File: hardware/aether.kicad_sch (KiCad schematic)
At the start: 41 parts, among them Q1 NPN, Q2 CSD17575Q3, Q3 CSD17575Q3, Q4 CSD17575Q3, Q5 CSD17575Q3, U1 USBLC6-2SC6

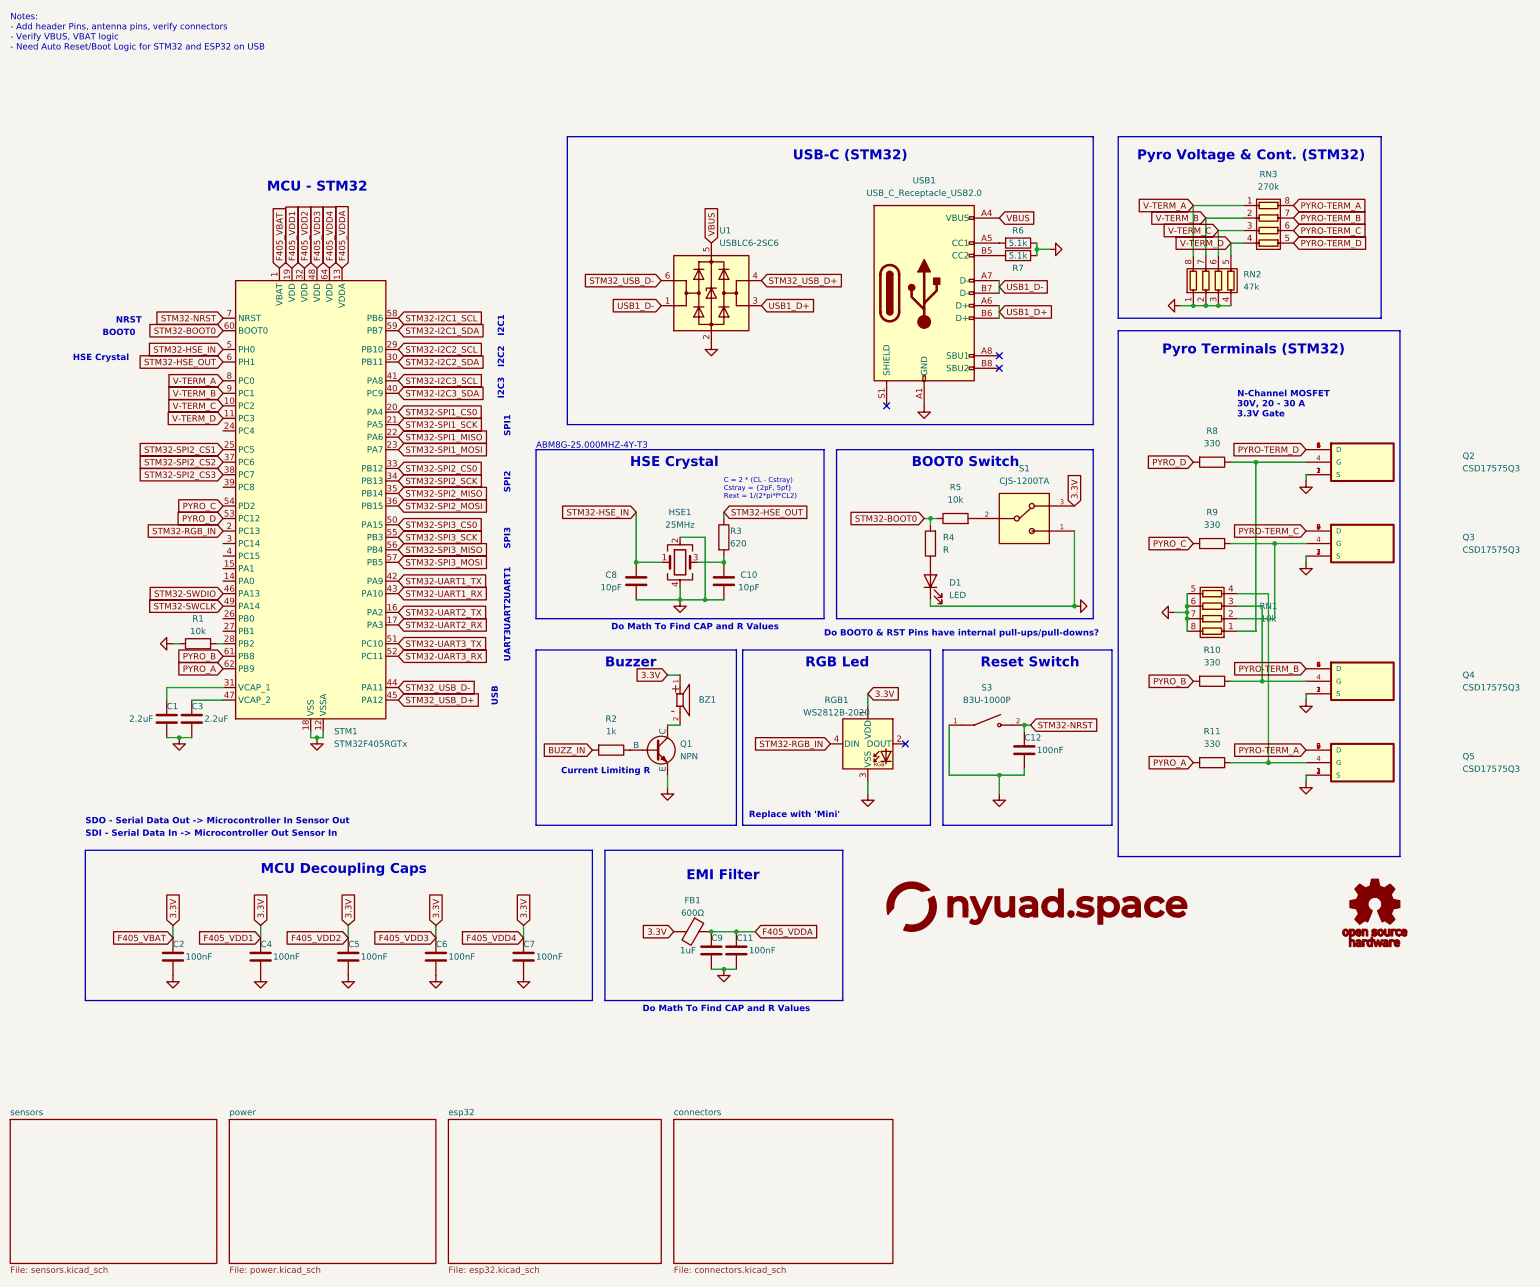
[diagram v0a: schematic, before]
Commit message: added BNO086
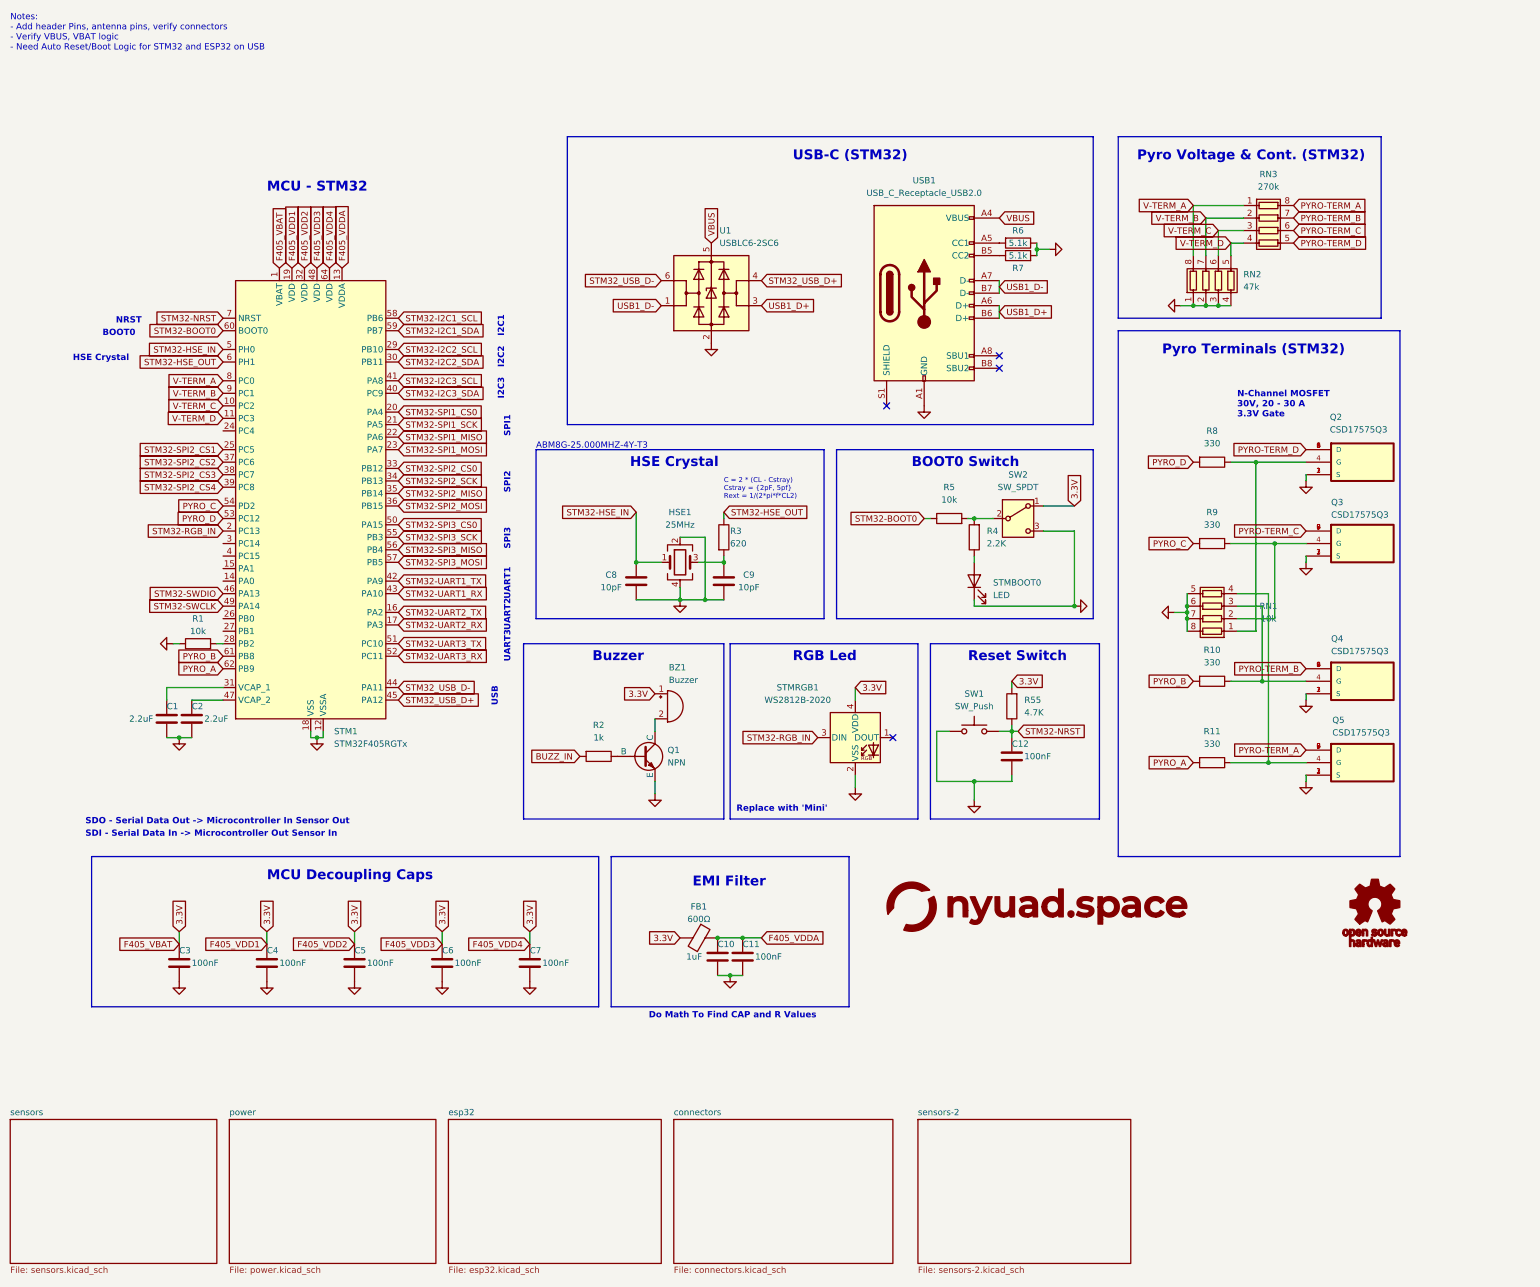
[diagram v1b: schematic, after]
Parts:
- removed BZ1: CSS-0575A-SMT, CSS-0575A-SMT:CUI_CSS-0575A-SMT, symbol CSS-0575A-SMT:CSS-0575A-SMT
- removed RGB1: WS2812B-2020, LED_SMD:LED_WS2812B-2020_PLCC4_2.0x2.0mm, symbol LED:WS2812B
- removed S1: CJS-1200TA, CJS-1200TA:SW_CJS-1200TA, symbol CJS-1200TA:CJS-1200TA
- removed S3: B3U-1000P, B3U-1000P:SW_B3U-1000P, symbol B3U-1000P:B3U-1000P
- added BZ1: Buzzer, symbol Device:Buzzer
- added R55: 4.7K, symbol Device:R
- added STMRGB1: WS2812B-2020, symbol LED:WS2812B-2020
- added SW1: SW_Push, symbol Switch:SW_Push
- added SW2: SW_SPDT, symbol Switch:SW_SPDT
- FB1: footprint Inductor_SMD:L_0402_1005Metric -> (none)
- HSE1: footprint Crystal:Crystal_SMD_Abracon_ABM8G-4Pin_3.2x2.5mm -> (none)
- Q1: footprint Package_TO_SOT_SMD:SOT-23 -> (none)
- Q2, Q3, Q4, Q5: footprint CSD17575Q3:TRANS_CSD17308Q3 -> (none)
- R1, R10, R11, R2, R3, R5, R6, R7, R8, R9: footprint Resistor_SMD:R_0603_1608Metric -> (none)
- R4: value R -> 2.2K; footprint Resistor_SMD:R_0603_1608Metric -> (none)
- RN1: footprint YC164-JR-0710KL:RESCAXE80P320X160X70-8N -> (none)
- RN2: footprint YC164-JR-0747KL:RESCAXE80P320X160X70-8N -> (none)
- RN3: footprint 742C083274JP:RESCAV80P320X160X70-8N -> (none)
- STM1: footprint Package_QFP:LQFP-64_10x10mm_P0.5mm -> (none)
- STMBOOT0: renamed from D1; footprint LED_SMD:LED_0603_1608Metric -> (none)
- U1: footprint Package_TO_SOT_SMD:SOT-23-6 -> (none)
- USB1: footprint Connector_USB:USB_C_Receptacle_GCT_USB4105-xx-A_16P_TopMnt_Horizontal -> (none)
- renumbered C9 to C10, C3 to C2, C2 to C3, C10 to C9
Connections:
- net 3.3V: now also BZ1.1 (+), R55.2, STMRGB1.4 (VDD), SW2.1 (A)
- net GND: now also STMRGB1.2 (VSS), SW1.1, SW2.3 (C)
- net STM32-BOOT0: no longer R4.2
- net STM32-NRST: now also R55.1, SW1.2
- net STM32-RGB_IN: now also STMRGB1.3 (DIN)
- net STM32-SPI2_CS4: now reaches STM1.39 (PC8)
- net at R5.2: now also R4.2, SW2.2 (B)
- net at Q1.1 (C): now also BZ1.2 (-)
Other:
- added sheet sensors-2 (sensors-2.kicad_sch)
- note removed: "Current Limiting R"
- note removed: "Do BOOT0 & RST Pins have internal pull-ups/pull-downs?"
- moved on the sheet: C10, C11, C12, C3, C4, C5, C6, C7, FB1, Q1, R2, R4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

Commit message: rev2 component placement
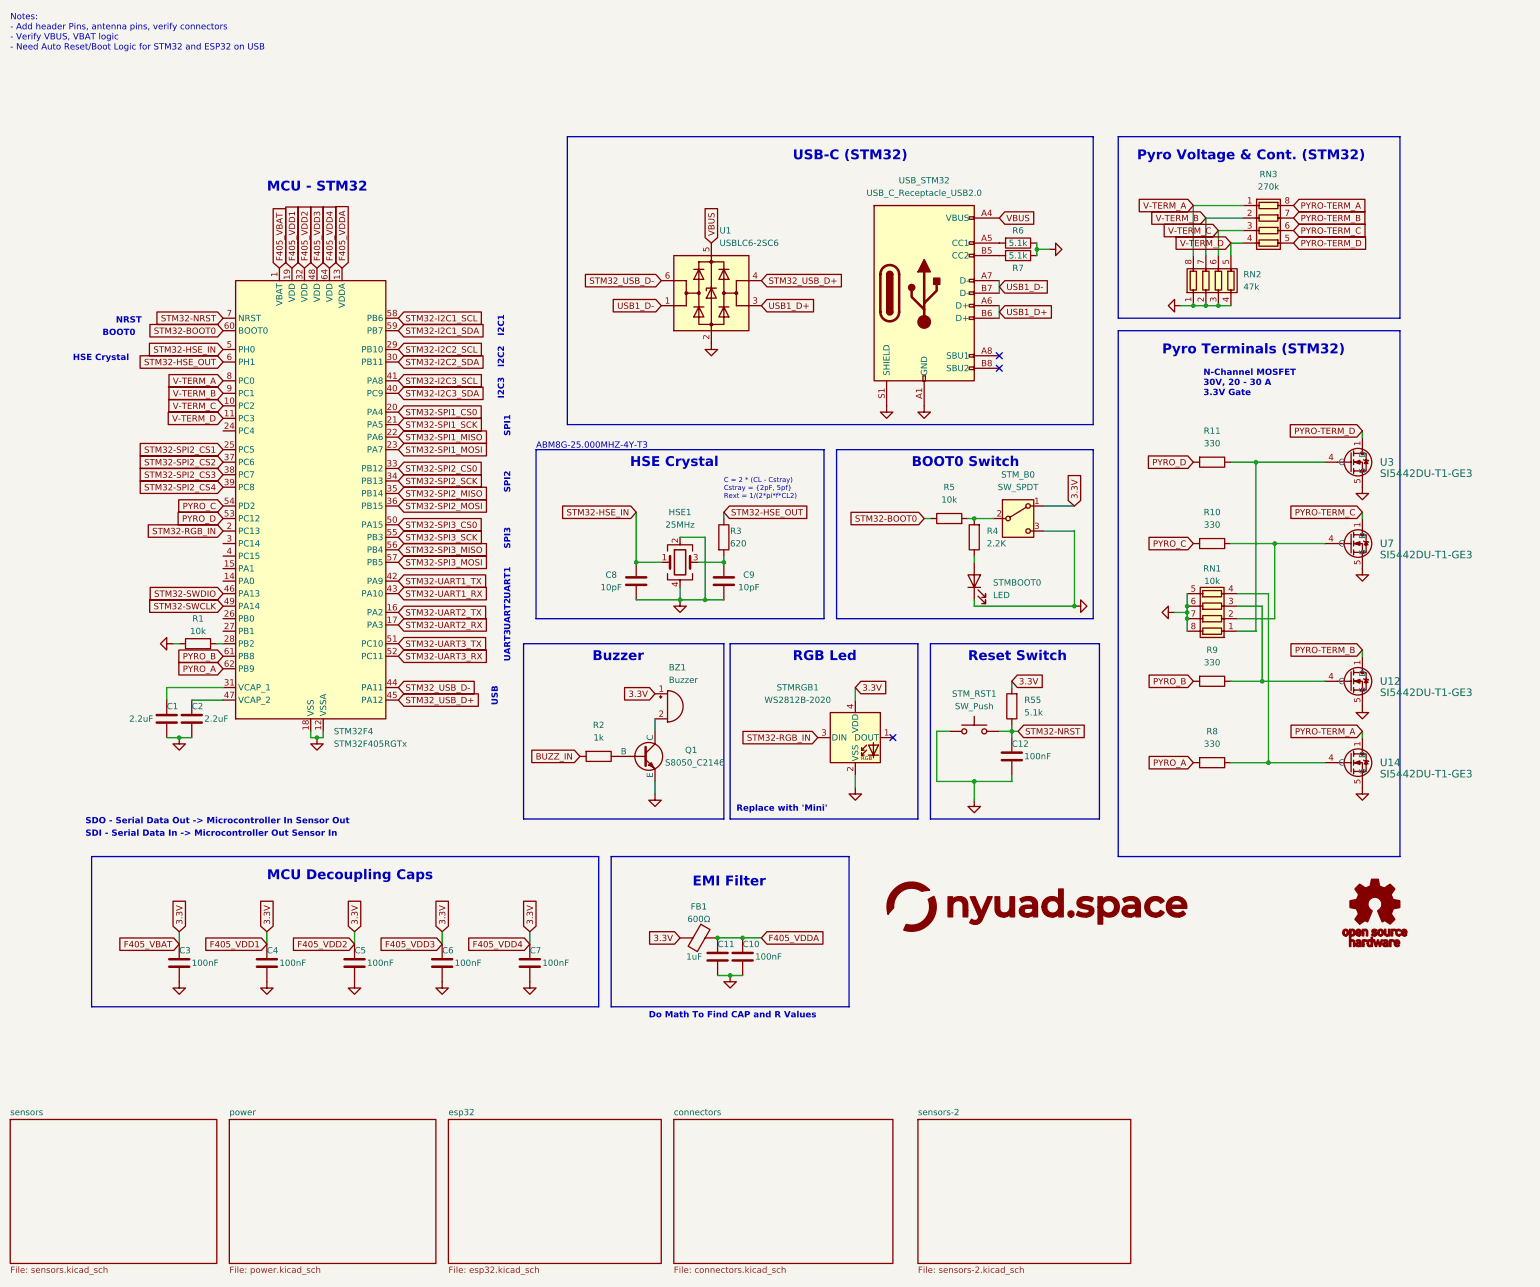
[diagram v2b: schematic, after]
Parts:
- removed Q2, Q3, Q4, Q5: CSD17575Q3, symbol CSD17575Q3:CSD17575Q3
- added U12, U14, U3, U7: SI5442DU-T1-GE3, SI5442DU_T1_GE3:SON_8DU-T1-GE3_VIS, symbol SI5442DU_T1_GE3:SI5442DU-T1-GE3
- BZ1: footprint (none) -> CSS-0575B-SMT:CUI_CSS-0575B-SMT
- FB1: footprint (none) -> Inductor_SMD:L_0402_1005Metric
- HSE1: footprint (none) -> Crystal:Crystal_SMD_Abracon_ABM8G-4Pin_3.2x2.5mm
- Q1: value NPN -> S8050_C2146; footprint (none) -> Package_TO_SOT_SMD:SOT-23-3
- R1, R2, R5, R6, R7: footprint (none) -> Resistor_SMD:R_0402_1005Metric
- R10: renamed from R9; footprint (none) -> Resistor_SMD:R_0402_1005Metric
- R11: renamed from R8; footprint (none) -> Resistor_SMD:R_0402_1005Metric
- R3, R4: footprint (none) -> Resistor_SMD:R_0603_1608Metric
- R55: value 4.7K -> 5.1k; footprint (none) -> Resistor_SMD:R_0402_1005Metric
- R8: renamed from R11; footprint (none) -> Resistor_SMD:R_0402_1005Metric
- R9: renamed from R10; footprint (none) -> Resistor_SMD:R_0402_1005Metric
- RN1, RN2, RN3: footprint (none) -> Resistor_SMD:R_Array_Convex_4x0402
- STM32F4: renamed from STM1; footprint (none) -> Package_QFP:LQFP-64_10x10mm_P0.5mm
- STMBOOT0: footprint (none) -> LED_SMD:LED_0603_1608Metric
- STMRGB1: footprint (none) -> LED_SMD:LED_WS2812B-2020_PLCC4_2.0x2.0mm
- STM_B0: renamed from SW2; footprint (none) -> Button_Switch_SMD:SW_SPDT_PCM12
- STM_RST1: renamed from SW1; footprint (none) -> Button_Switch_SMD:SW_SPST_B3U-1000P
- U1: footprint (none) -> Package_TO_SOT_SMD:SOT-23-6
- USB_STM32: renamed from USB1; footprint (none) -> Connector_USB:USB_C_Receptacle_G-Switch_GT-USB-7010ASV
- renumbered C11 to C10, C10 to C11
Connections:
- net GND: now also USB_STM32.S1 (SHIELD), U12.5 (S), U12.9 (S), U14.5 (S), U14.9 (S), U3.5 (S), U3.9 (S), U7.5 (S), U7.9 (S)
- net PYRO-TERM_A: now also U14.1 (D)
- net PYRO-TERM_B: now also U12.1 (D)
- net PYRO-TERM_C: now also U7.1 (D)
- net PYRO-TERM_D: now also U3.1 (D)
- net at R11.1, RN1.1 (R1.1): now also U3.4 (G)
- net at R10.1, RN1.2 (R2.1): now also U7.4 (G)
- net at R9.1, RN1.3 (R3.1): now also U12.4 (G)
- net at R8.1, RN1.4 (R4.1): now also U14.4 (G)
- no-connect marks 4 -> 3

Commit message: updated files
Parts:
- removed BZ1: Buzzer, CSS-0575B-SMT:CUI_CSS-0575B-SMT, symbol Device:Buzzer
- removed STM_B0: SW_SPDT, Button_Switch_SMD:SW_SPDT_PCM12, symbol Switch:SW_SPDT
- added BUZ1: FST-5030, FUET-5030:BUZ-SMD_FST-5030, symbol FST-5030:FST-5030
- added STM_B0: SS-3292S-L2-B, SS-3292S-L2-B:SW-SMD_SS-3292S-L2-B, symbol SS-3292S-L2-B:SS-3292S-L2-B
- U12, U3, U7: value SI5442DU-T1-GE3 -> SI5448DU-T1-GE3
- U14: value SI5442DU-T1-GE3 -> SI5448DU-T1-GE3; now left out of the parts list
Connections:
- net 3.3V: now also BUZ1.1 (+), STM_B0.1
- net GND: now also STM_B0.3, STM_B0.EH
- net STM32-RGB_IN: now also STM32F4.15 (PA1); no longer STM32F4.2 (PC13)
- net at Q1.1 (C): now also BUZ1.2
- net at R4.2, R5.2: now also STM_B0.2
- no-connect marks 3 -> 4
